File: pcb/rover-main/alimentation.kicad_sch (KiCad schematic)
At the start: 0 parts

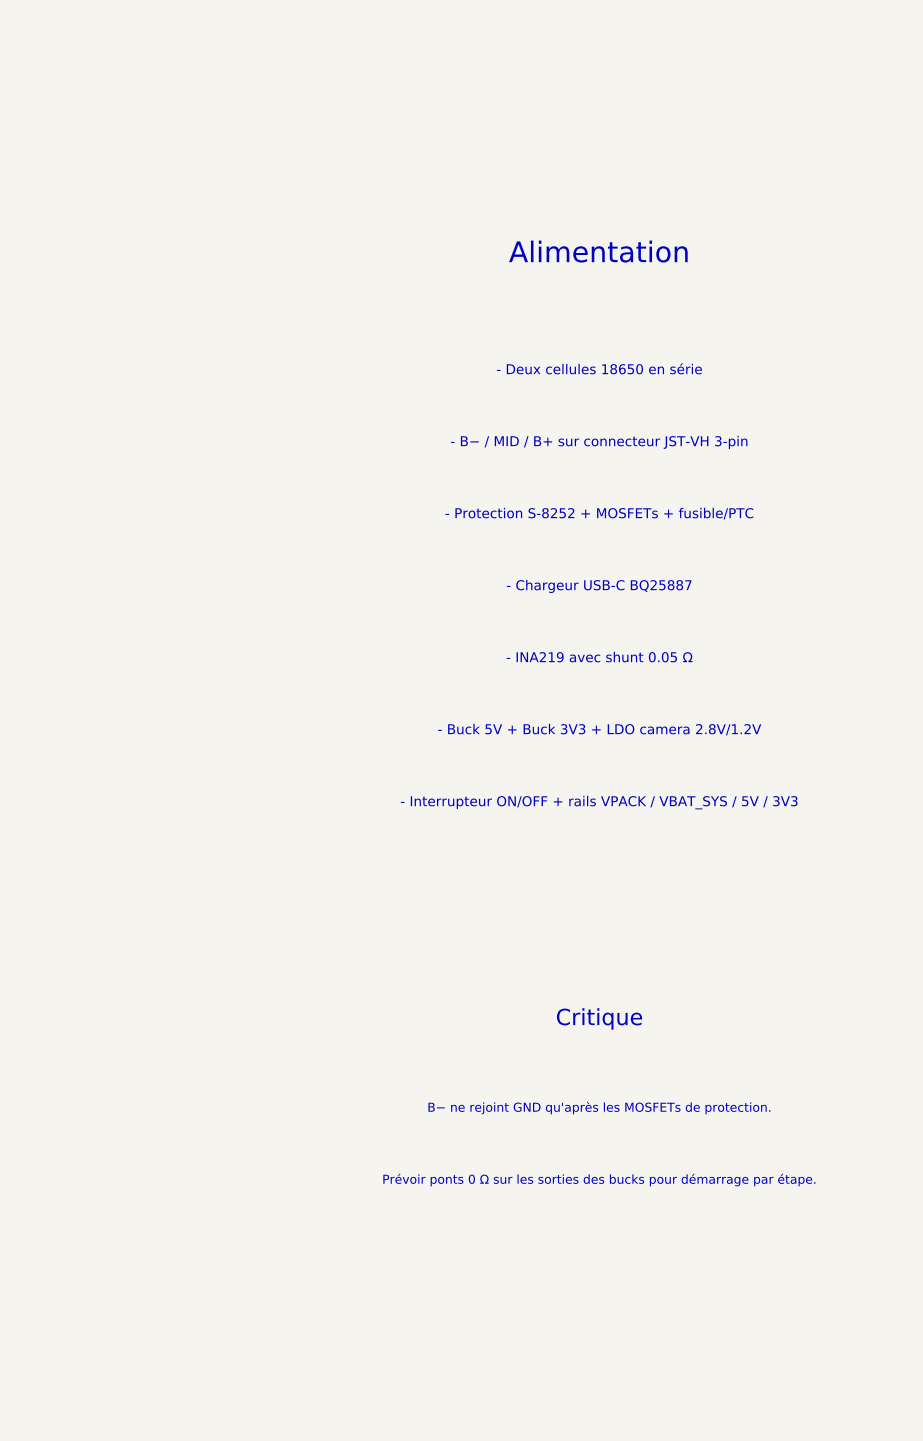
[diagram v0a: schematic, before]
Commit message: Add a more concrete KiCad schematic draft with key blocks and real net names for the Rover PCB design.
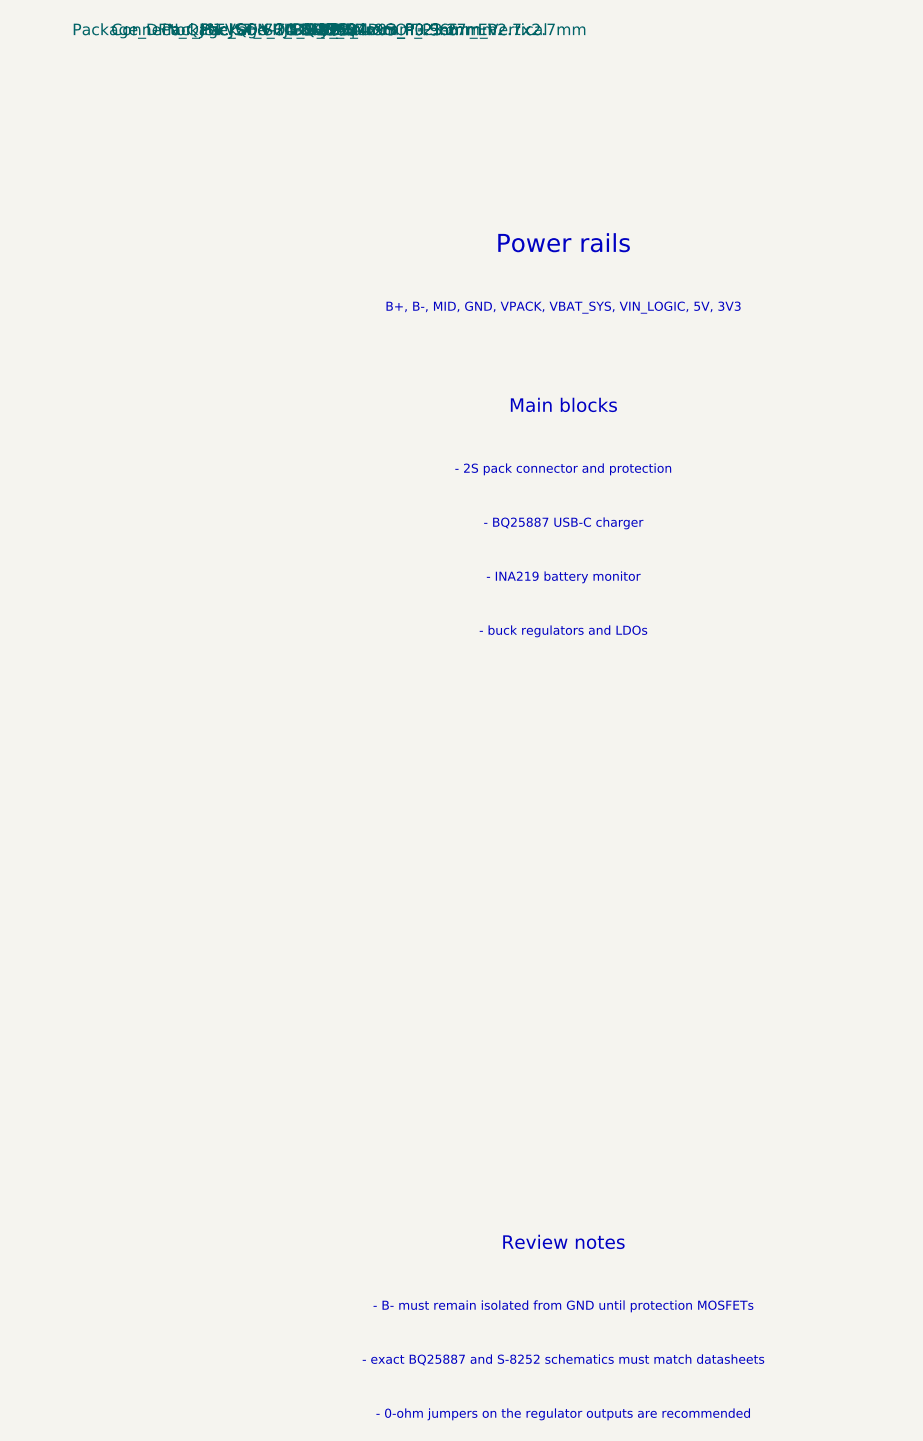
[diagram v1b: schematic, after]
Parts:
- added J1: JST-VH 3pin, Connector_JST:JST_VH_B3P-VH_1x03_P3.96mm_Vertical, symbol Connector_Generic:Conn_01x03
- added U7: INA219, Package_SO:SOIC-8_3.9x4.9mm_P1.27mm, symbol Power_Management:INA219
- added U8: BQ25887, Package_DFN_QFN:VQFN-24-1EP_4x4mm_P0.5mm_EP2.7x2.7mm, symbol Power_Management:BQ25887
- added U9: S-8252, Package_TO_SOT_SMD:SOT-23-6, symbol Battery_Management:ABLIC_S-8252
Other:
- note added: "- 0-ohm jumpers on the regulator outputs are recommended"
- note added: "- 2S pack connector and protection"
- note added: "- B- must remain isolated from GND until protection MOSFETs"
- note added: "- BQ25887 USB-C charger"
- note added: "- INA219 battery monitor"
- note added: "- buck regulators and LDOs"
- note added: "- exact BQ25887 and S-8252 schematics must match datasheets"
- note added: "B+, B-, MID, GND, VPACK, VBAT_SYS, VIN_LOGIC, 5V, 3V3"
- note added: "Main blocks"
- note added: "Power rails"
- note added: "Review notes"
- note removed: "- Buck 5V + Buck 3V3 + LDO camera 2.8V/1.2V"
- note removed: "- B− / MID / B+ sur connecteur JST-VH 3-pin"
- note removed: "- Chargeur USB-C BQ25887"
- note removed: "- Deux cellules 18650 en série"
- note removed: "- INA219 avec shunt 0.05 Ω"
- note removed: "- Interrupteur ON/OFF + rails VPACK / VBAT_SYS / 5V / 3V3"
- note removed: "- Protection S-8252 + MOSFETs + fusible/PTC"
- note removed: "Alimentation"
- note removed: "B− ne rejoint GND qu'après les MOSFETs de protection."
- note removed: "Critique"
- note removed: "Prévoir ponts 0 Ω sur les sorties des bucks pour démarrage par étape."
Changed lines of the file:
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@@
 (kicad_sch
-  (version 20250114)
-  (generator "KiCad")
+  (version 20211014)
+  (generator "eeschema")
   (paper "A4")
   (title_block
     (title "Rover PCB - alimentation")
     (date "2026-10-13")
-    (rev "0.1")
+    (rev "0.2")
     (company "Rover Project")
-    (comment 1 "Draft only - validate exact values with datasheets")
+    (comment 1 "Draft schematic - validate BMS and regulator application circuits")
   )
-  (text "Alimentation" (at 30 25 0)
-    (effects (font (size 2.3 2.3) (thickness 0.3)))
+  (text "Power rails" (at 26 24 0)
+    (effects (font (size 2.0 2.0) (thickness 0.2)))
   )
-  (text "- Deux cellules 18650 en série" (at 30 38 0)
-    (effects (font (size 1.1 1.1)))
-  )
-  (text "- B− / MID / B+ sur connecteur JST-VH 3-pin" (at 30 46 0)
-    (effects (font (size 1.1 1.1)))
-  )
-  (text "- Protection S-8252 + MOSFETs + fusible/PTC" (at 30 54 0)
-    (effects (font (size 1.1 1.1)))
-  )
-  (text "- Chargeur USB-C BQ25887" (at 30 62 0)
-    (effects (font (size 1.1 1.1)))
-  )
-  (text "- INA219 avec shunt 0.05 Ω" (at 30 70 0)
-    (effects (font (size 1.1 1.1)))
-  )
-  (text "- Buck 5V + Buck 3V3 + LDO camera 2.8V/1.2V" (at 30 78 0)
-    (effects (font (size 1.1 1.1)))
-  )
-  (text "- Interrupteur ON/OFF + rails VPACK / VBAT_SYS / 5V / 3V3" (at 30 86 0)
-    (effects (font (size 1.1 1.1)))
-  )
-  (text "Critique" (at 30 110 0)
-    (effects (font (size 1.8 1.8) (thickness 0.25)))
-  )
-  (text "B− ne rejoint GND qu'après les MOSFETs de protection." (at 30 120 0)
+  (text "B+, B-, MID, GND, VPACK, VBAT_SYS, VIN_LOGIC, 5V, 3V3" (at 26 31 0)
     (effects (font (size 1.0 1.0)))
   )
-  (text "Prévoir ponts 0 Ω sur les sorties des bucks pour démarrage par étape." (at 30 128 0)
+  (text "Main blocks" (at 26 42 0)
+    (effects (font (size 1.5 1.5) (thickness 0.2)))
+  )
+  (text "- 2S pack connector and protection" (at 26 49 0)
     (effects (font (size 1.0 1.0)))
   )
+  (text "- BQ25887 USB-C charger" (at 26 55 0)
+    (effects (font (size 1.0 1.0)))
+  )
+  (text "- INA219 battery monitor" (at 26 61 0)
+    (effects (font (size 1.0 1.0)))
+  )
+  (text "- buck regulators and LDOs" (at 26 67 0)
+    (effects (font (size 1.0 1.0)))
+  )
+  (symbol
+    (lib_id "Connector_Generic:Conn_01x03")
+    (at 50 95 0)
+    (unit 1)
+    (in_bom yes)
+    (property "Reference" "J1")
+    (property "Value" "JST-VH 3pin")
+    (property "Footprint" "Connector_JST:JST_VH_B3P-VH_1x03_P3.96mm_Vertical")
+  )
+  (symbol
+    (lib_id "Battery_Management:ABLIC_S-8252")
+    (at 110 95 0)
+    (unit 1)
+    (in_bom yes)
+    (property "Reference" "U9")
+    (property "Value" "S-8252")
+    (property "Footprint" "Package_TO_SOT_SMD:SOT-23-6")
+  )
+  (symbol
+    (lib_id "Power_Management:BQ25887")
+    (at 180 95 0)
+    (unit 1)
+    (in_bom yes)
+    (property "Reference" "U8")
+    (property "Value" "BQ25887")
+    (property "Footprint" "Package_DFN_QFN:VQFN-24-1EP_4x4mm_P0.5mm_EP2.7x2.7mm")
+  )
+  (symbol
+    (lib_id "Power_Management:INA219")
+    (at 260 95 0)
+    (unit 1)
+    (in_bom yes)
+    (property "Reference" "U7")
+    (property "Value" "INA219")
+    (property "Footprint" "Package_SO:SOIC-8_3.9x4.9mm_P1.27mm")
+  )
+  (text "Review notes" (at 26 135 0)
+    (effects (font (size 1.5 1.5) (thickness 0.2)))
+  )
+  (text "- B- must remain isolated from GND until protection MOSFETs" (at 26 142 0)
+    (effects (font (size 1.0 1.0)))
+  )
+  (text "- exact BQ25887 and S-8252 schematics must match datasheets" (at 26 148 0)
+    (effects (font (size 1.0 1.0)))
+  )
+  (text "- 0-ohm jumpers on the regulator outputs are recommended" (at 26 154 0)
+    (effects (font (size 1.0 1.0)))
+  )
